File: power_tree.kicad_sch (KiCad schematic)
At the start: 16 parts, among them J3 BAT1_01x02_Pin, Q1 FDN340P, U6 TP4056-42-ESOP8, U7 AP2112K-3.3

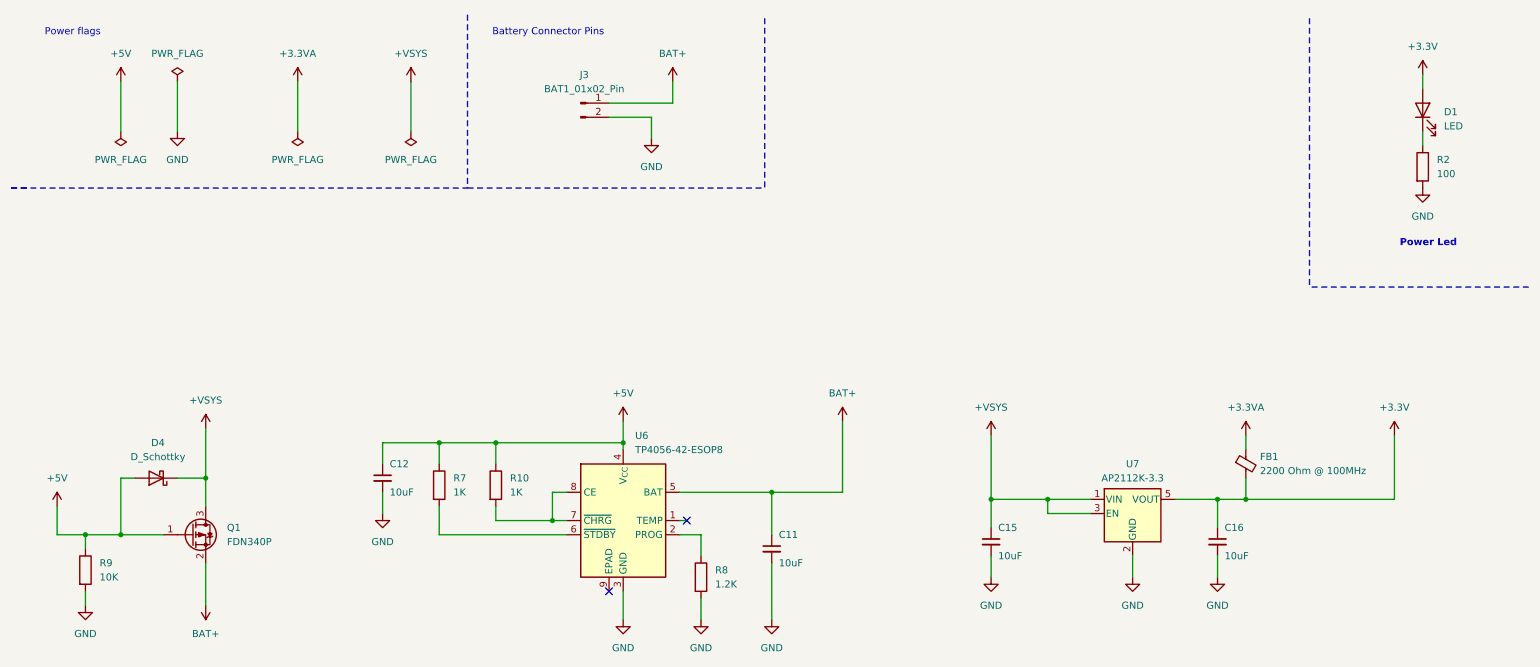
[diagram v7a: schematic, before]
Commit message: fix(fixed_annotation): sorted by x position
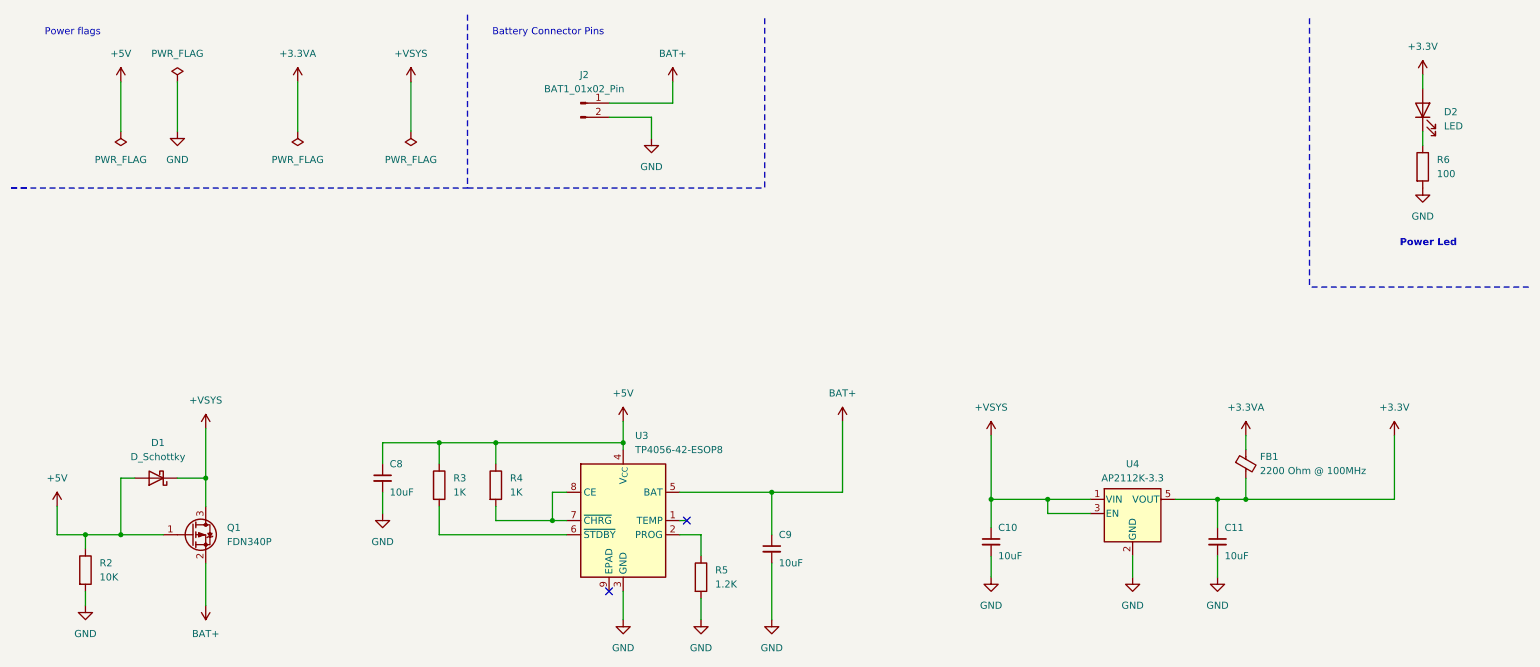
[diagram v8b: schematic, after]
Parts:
- renumbered C15 to C10, C16 to C11, C12 to C8, C11 to C9, D4 to D1, D1 to D2, J3 to J2, R9 to R2, R7 to R3, R10 to R4, R8 to R5, R2 to R6, U6 to U3, U7 to U4
